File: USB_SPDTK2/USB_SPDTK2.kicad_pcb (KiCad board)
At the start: 2 copper layers, 34 x 50 mm, 65 parts, among them J1 USB_B_Micro, J2 TagConnectTC2050, J3 Conn_02x08_Odd_Even, SW1 SW_Push, SW2 SW_Push, U1 LM27313XMF, U2 LP2985-3.3, U3 L293DD, U4 STM32F411RETx, U5 93LC66AT-IOT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

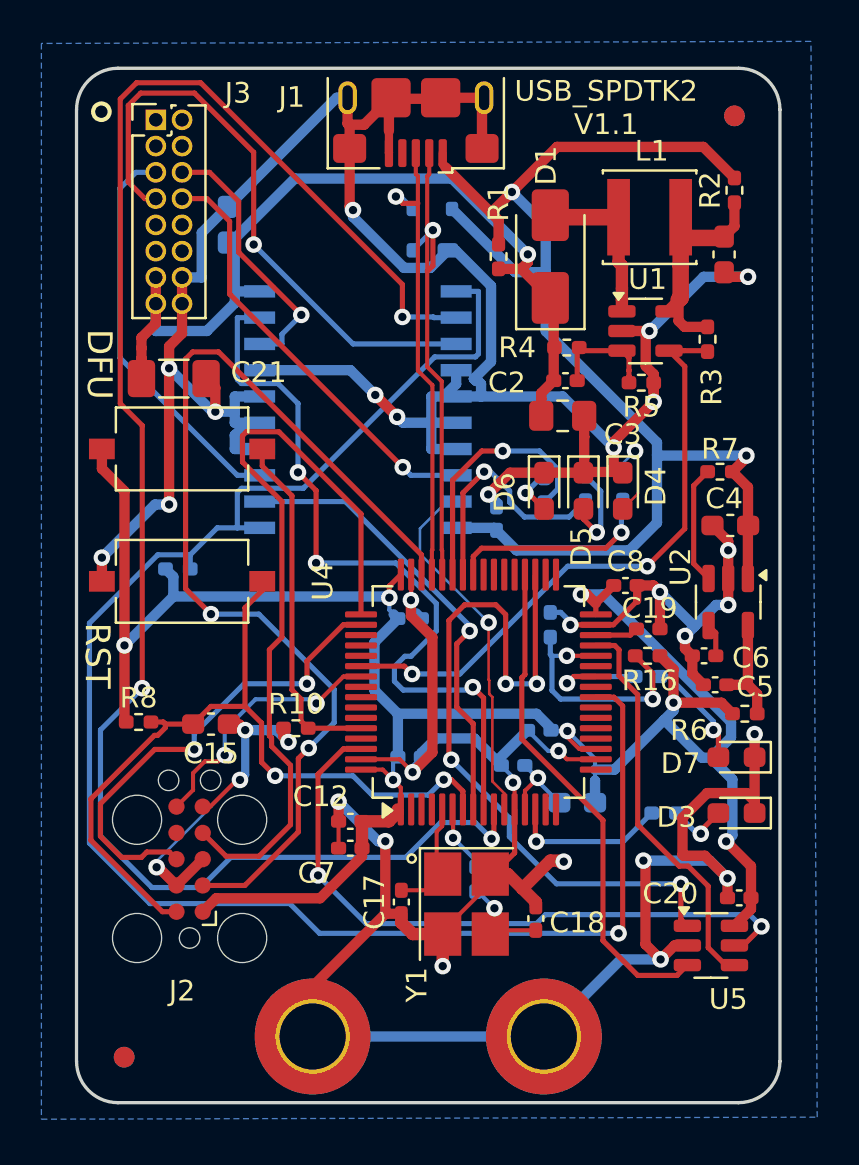
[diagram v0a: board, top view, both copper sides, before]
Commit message: Fix connector and C21 interference.
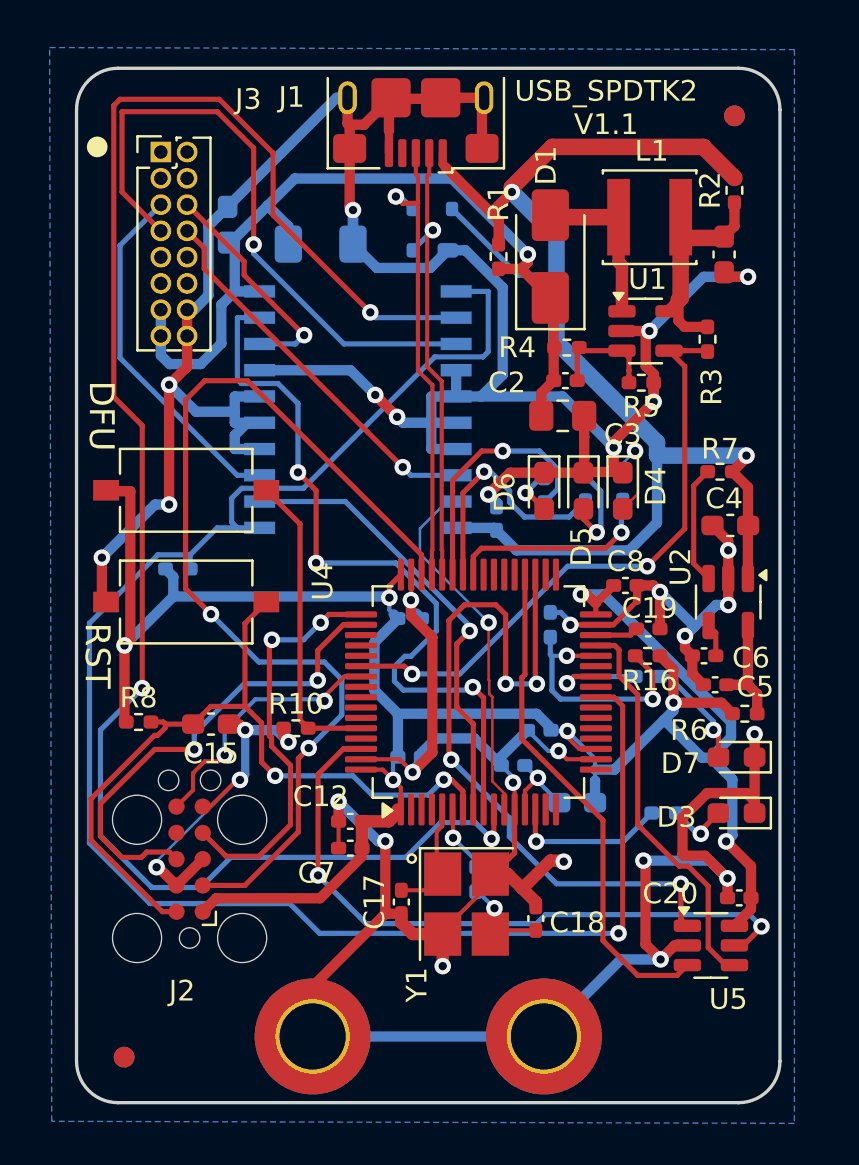
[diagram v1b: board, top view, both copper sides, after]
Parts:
- C21: moved to B.Cu
- moved C21 9.63 mm to (119.4, 72.2)
- moved SW2 2.01 mm to (112.9, 84.1)
- moved J3 1.58 mm to (111.7, 67.8)
- moved SW1 1.02 mm to (112.9, 89.5)
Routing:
- net /Controller/JTCK: track 37.9 -> 19.6 mm, vias 0 -> 2
- net S2D_OUT: track 20.8 -> 18.5 mm
- net Net-(U4-BOOT0): track 17.0 -> 14.9 mm
- net S1U_OUT: track 19.4 -> 17.3 mm
- net S1D_OUT: track 12.9 -> 11.0 mm
- net /Controller/USB-: track 24.2 -> 22.5 mm
- net /Controller/JTMS: track 50.2 -> 48.7 mm
- net VBUS: track 65.5 -> 66.8 mm
- net +3.3V: track 109.3 -> 108.1 mm
- net S2U_OUT: track 29.1 -> 30.3 mm
- net SW_Enable: track 81.6 -> 82.7 mm
- net Net-(J2-~{RESET}): track 38.9 -> 38.0 mm
- net GND: track 267.1 -> 268.0 mm, vias 33 -> 32
